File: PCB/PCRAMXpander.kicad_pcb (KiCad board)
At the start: 2 copper layers, 134.6 x 97.8 mm, 22 parts, among them J1 Bus_ISA_16bit, U1 ATF16V8B-15PU, U2 SN74LVCR16245ADGGR, U3 SN74LVC16244ADGGR, U4 SN74LVC16244ADGGR, U5 AS6C3216A-55TIN, U6 AS6C3216A-55TIN

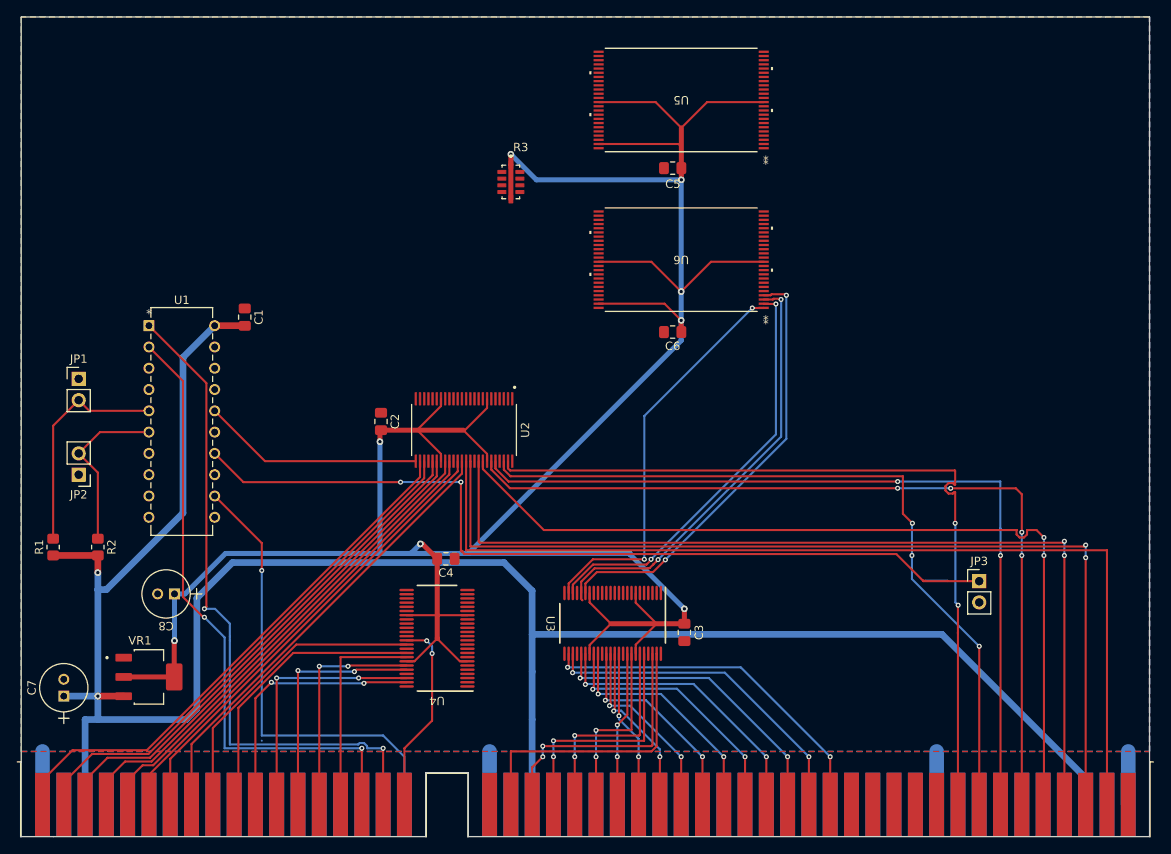
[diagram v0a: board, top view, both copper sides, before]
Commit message: More manual routing
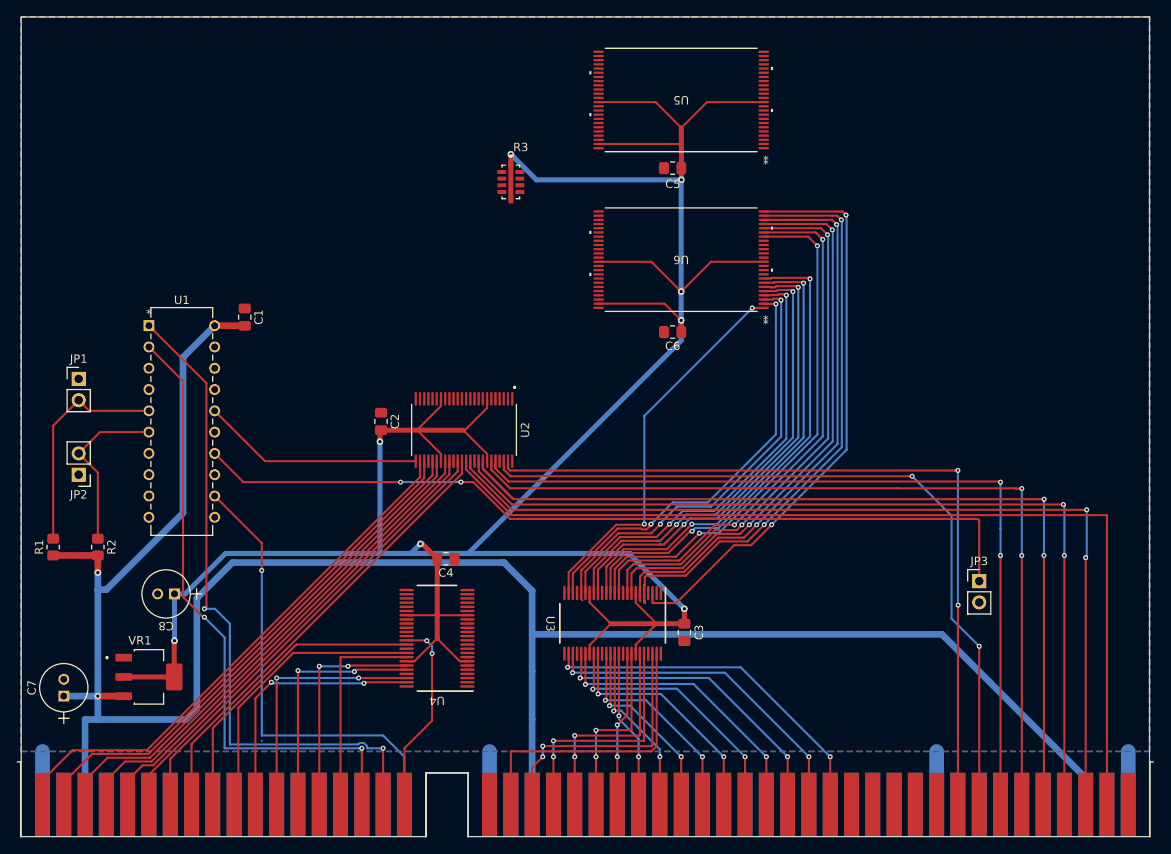
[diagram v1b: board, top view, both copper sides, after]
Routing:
- net A2: track 0.00 -> 70.9 mm, vias 0 -> 2
- net A1: track 0.00 -> 69.9 mm, vias 0 -> 2
- net A3: track 0.00 -> 69.1 mm, vias 0 -> 2
- net A4: track 0.00 -> 66.6 mm, vias 0 -> 2
- net A5: track 0.00 -> 65.5 mm, vias 0 -> 2
- net A6: track 0.00 -> 64.5 mm, vias 0 -> 2
- net A7: track 0.00 -> 63.1 mm, vias 0 -> 2
- net A8: track 0.00 -> 57.7 mm, vias 0 -> 2
- net A9: track 0.00 -> 56.5 mm, vias 0 -> 2
- net A10: track 0.00 -> 55.4 mm, vias 0 -> 2
- net A11: track 0.00 -> 54.2 mm, vias 0 -> 2
- net Net-(J1-DB4): track 104.5 -> 111.9 mm
- net Net-(JP3-A): track 105.4 -> 101.8 mm
- net Net-(J1-DB7): track 117.4 -> 114.3 mm
- net Net-(J1-DB6): track 114.6 -> 111.7 mm
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
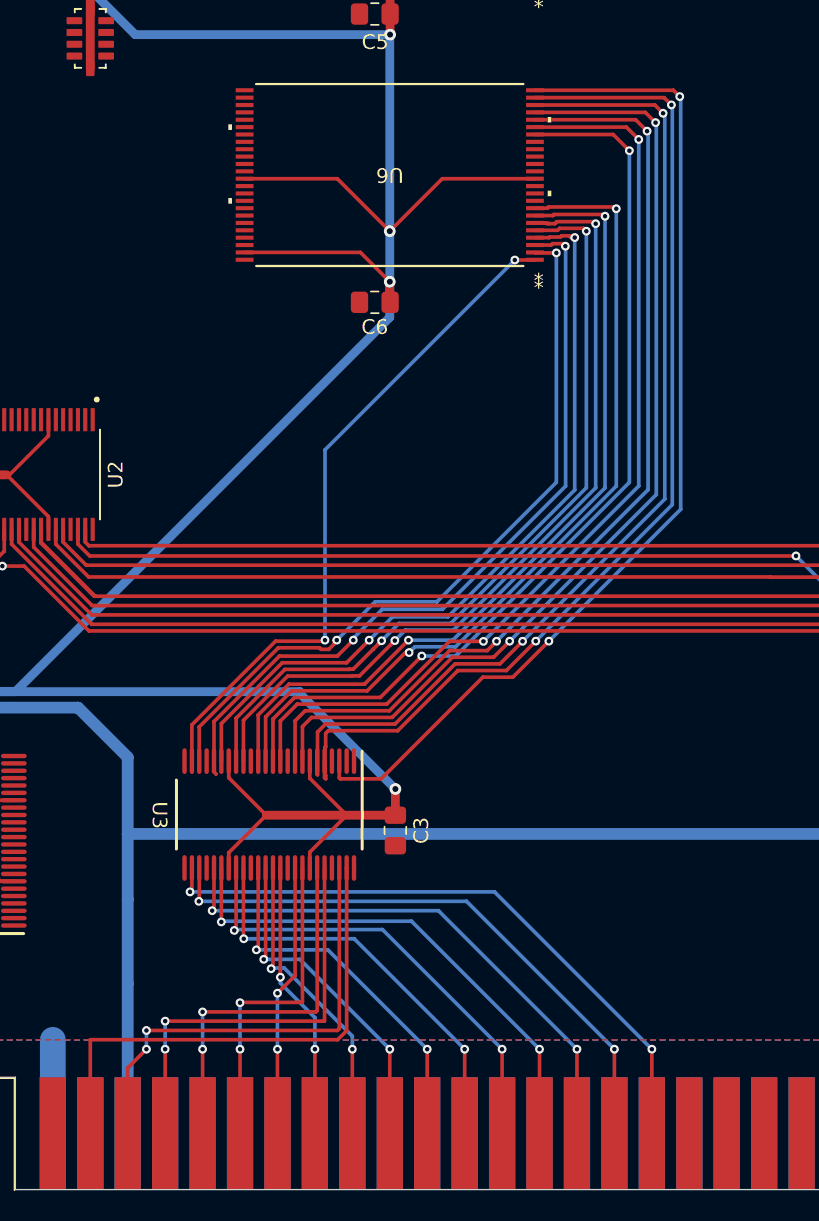
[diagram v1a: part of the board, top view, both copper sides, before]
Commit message: Moving U3 for more routing space
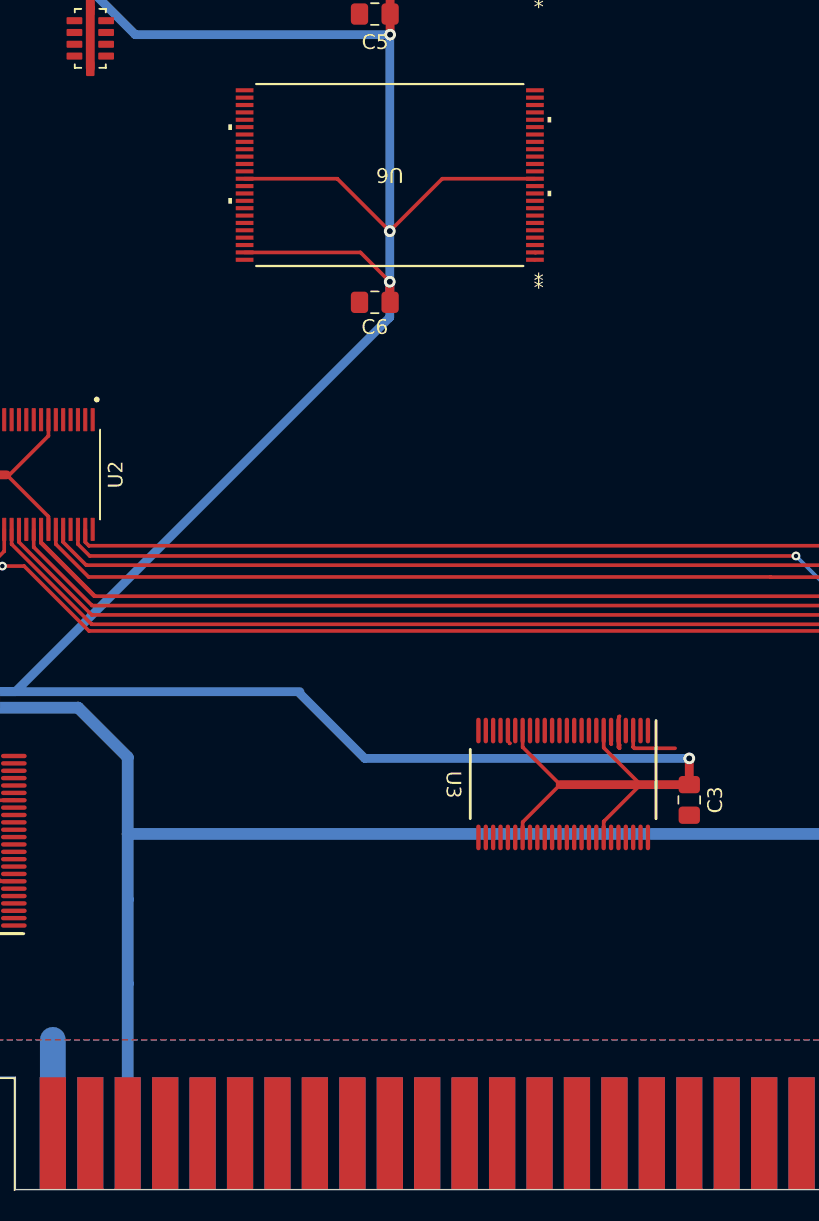
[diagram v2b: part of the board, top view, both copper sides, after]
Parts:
- moved U3 20.0 mm to (154.0, 124.9)
- moved C3 20.0 mm to (162.6, 126.0)
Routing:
- net A3: track 69.1 -> 0.93 mm, vias 2 -> 0
- net A2: track 70.9 -> 3.45 mm, vias 2 -> 0
- net A4: track 66.6 -> 0.00 mm, vias 2 -> 0
- net A1: track 69.9 -> 4.00 mm, vias 2 -> 0
- net A5: track 65.5 -> 0.00 mm, vias 2 -> 0
- net A6: track 64.5 -> 0.00 mm, vias 2 -> 0
- net A7: track 63.1 -> 0.00 mm, vias 2 -> 0
- net A8: track 57.7 -> 0.00 mm, vias 2 -> 0
- net A9: track 56.5 -> 0.00 mm, vias 2 -> 0
- net A10: track 55.4 -> 0.00 mm, vias 2 -> 0
- net A11: track 54.2 -> 0.00 mm, vias 2 -> 0
- net A12: track 53.0 -> 0.00 mm, vias 2 -> 0
- net A13: track 52.0 -> 0.00 mm, vias 2 -> 0
- net A14: track 50.7 -> 0.06 mm, vias 2 -> 0
- net A15: track 46.4 -> 0.02 mm, vias 2 -> 0
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
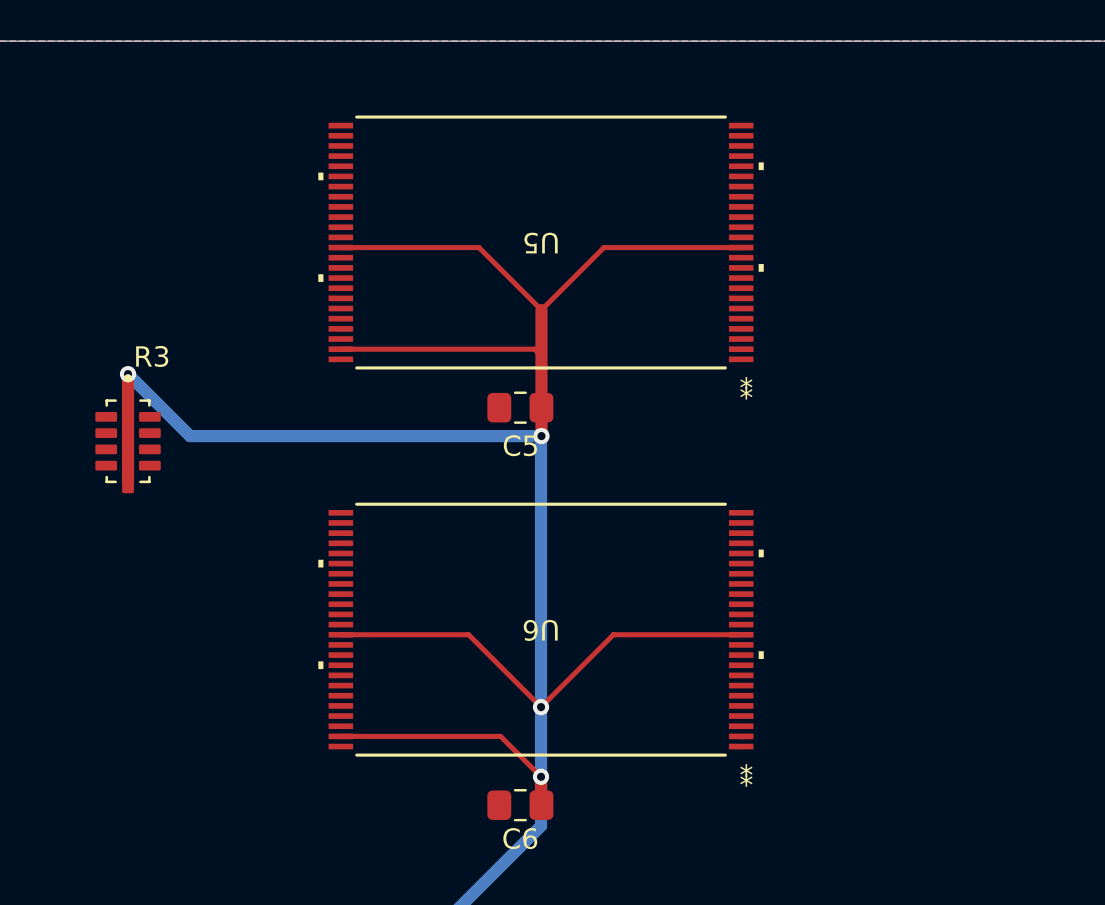
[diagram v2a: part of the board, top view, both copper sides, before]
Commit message: Ram wired up
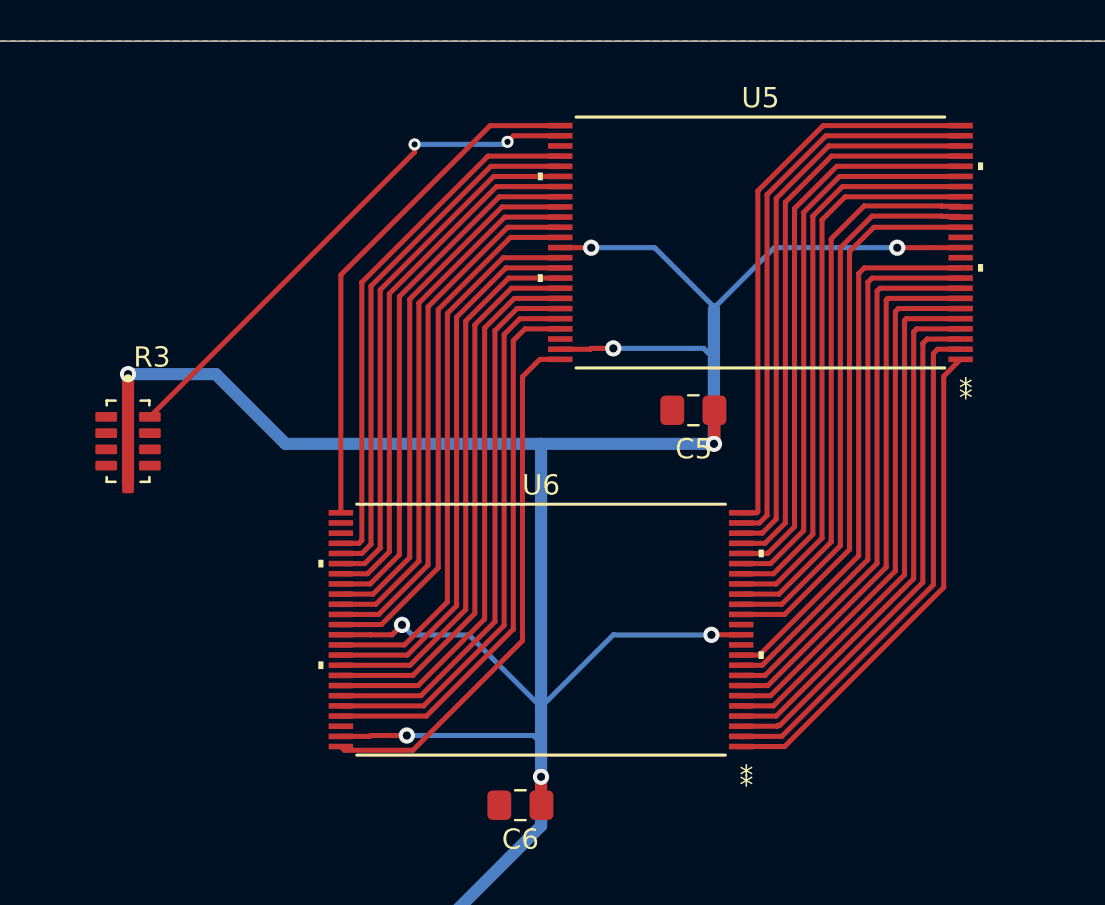
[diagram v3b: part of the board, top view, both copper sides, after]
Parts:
- moved U5 10.8 mm to (153.0, 64.5)
- moved C5 8.51 mm to (149.7, 72.8)
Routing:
- net A2: track 3.45 -> 31.4 mm
- net A1: track 4.00 -> 31.9 mm
- net A4: track 0.00 -> 27.9 mm
- net A3: track 0.93 -> 28.9 mm
- net A7: track 0.00 -> 27.9 mm
- net A6: track 0.00 -> 27.9 mm
- net A5: track 0.00 -> 27.9 mm
- net A17: track 0.00 -> 27.9 mm
- net A18: track 0.00 -> 27.5 mm
- net LB: track 0.00 -> 27.3 mm
- net UB: track 0.00 -> 27.3 mm
- net D7: track 0.00 -> 27.1 mm
- net D6: track 0.00 -> 27.1 mm
- net D14: track 0.00 -> 27.1 mm
- net D15: track 0.00 -> 27.0 mm
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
